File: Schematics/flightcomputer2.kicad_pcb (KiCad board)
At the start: 4 copper layers, 80 x 80 mm, 105 parts, among them J1 Microsemi_FlashPro-JTAG-10, J10 Pyro, J2 Pyro, J4 Drouge, J5 Conn_01x05_Pin, J6 Conn_01x05_Pin, J7 Conn_Coaxial_Small, J8 Micro_SD_Card, J9 USB_C_Receptacle_USB2.0_16P, Q1 IRLML2502TRPBF, Q2 IRLML2502TRPBF, Q3 BC817, Q4 IRLML2502TRPBF, Q6 Q_PMOS_GSD, SW1 SAMZO G4R0015010, SW2 SAMZO G4R0015010, U1 STM32F405RGT6, U2 SN65HVD230, U3 PowerIn, U4 LDL1117-3.3, U5 RFM95W-915S2, U6 Bosch BMP388, U7 LSM6DS3TR-C, U8 W25Q128JVP, U9 H3LIS331DL, Y1 8mhz

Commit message: dfm sent for ordering
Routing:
- net /FlashMemory/SPI_MOSI: track 42.3 -> 43.5 mm
- net /MCU/SWCLK: track 69.0 -> 68.0 mm
- net /GPS/GPS2_TX: track 41.0 -> 40.3 mm
- net /GPS/GPS2_RX: track 44.9 -> 44.2 mm
- net /GPS/RESET2: track 49.2 -> 49.8 mm
- net /GPS/RESET1: track 62.5 -> 62.0 mm
- net /FlashMemory/SPICLK: track 42.0 -> 41.5 mm
- net GND: track 153.8 -> 154.0 mm, vias 88 -> 87

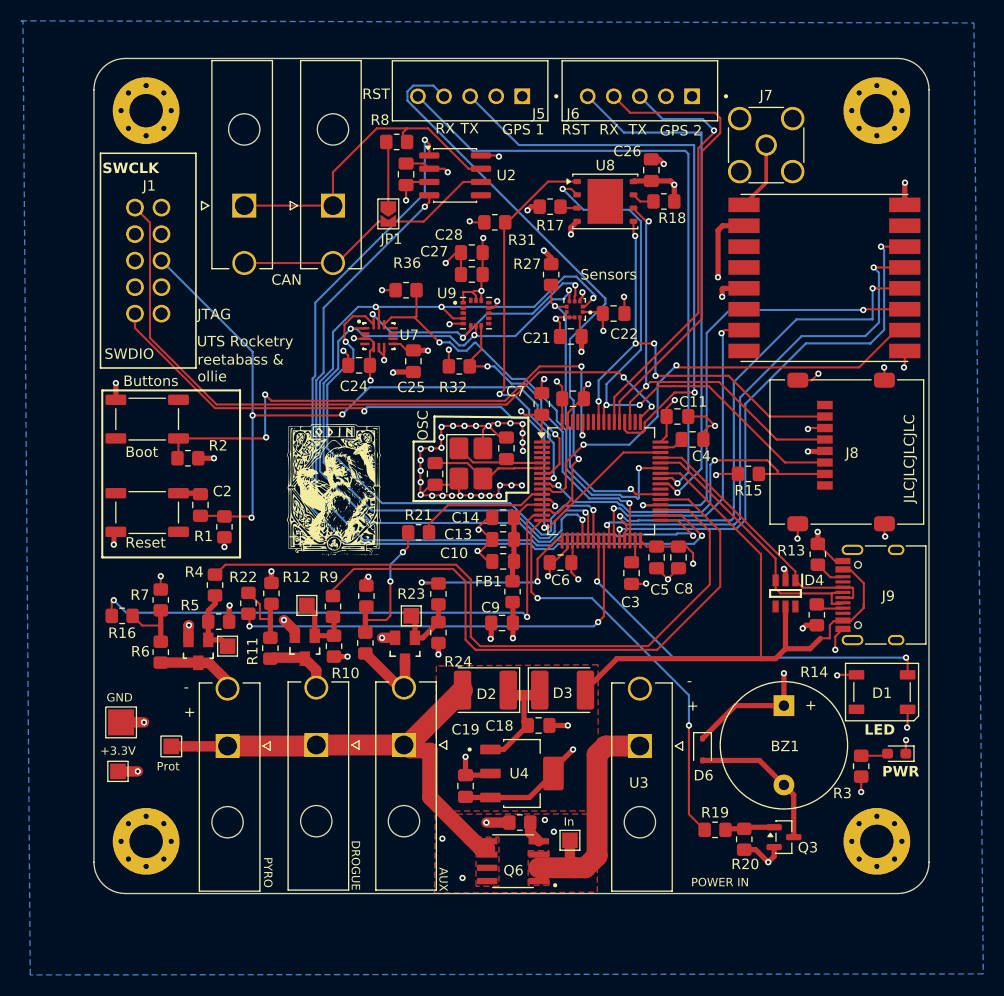
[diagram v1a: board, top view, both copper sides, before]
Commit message: added DIO0 and DIO2 pins to read lora module outputs
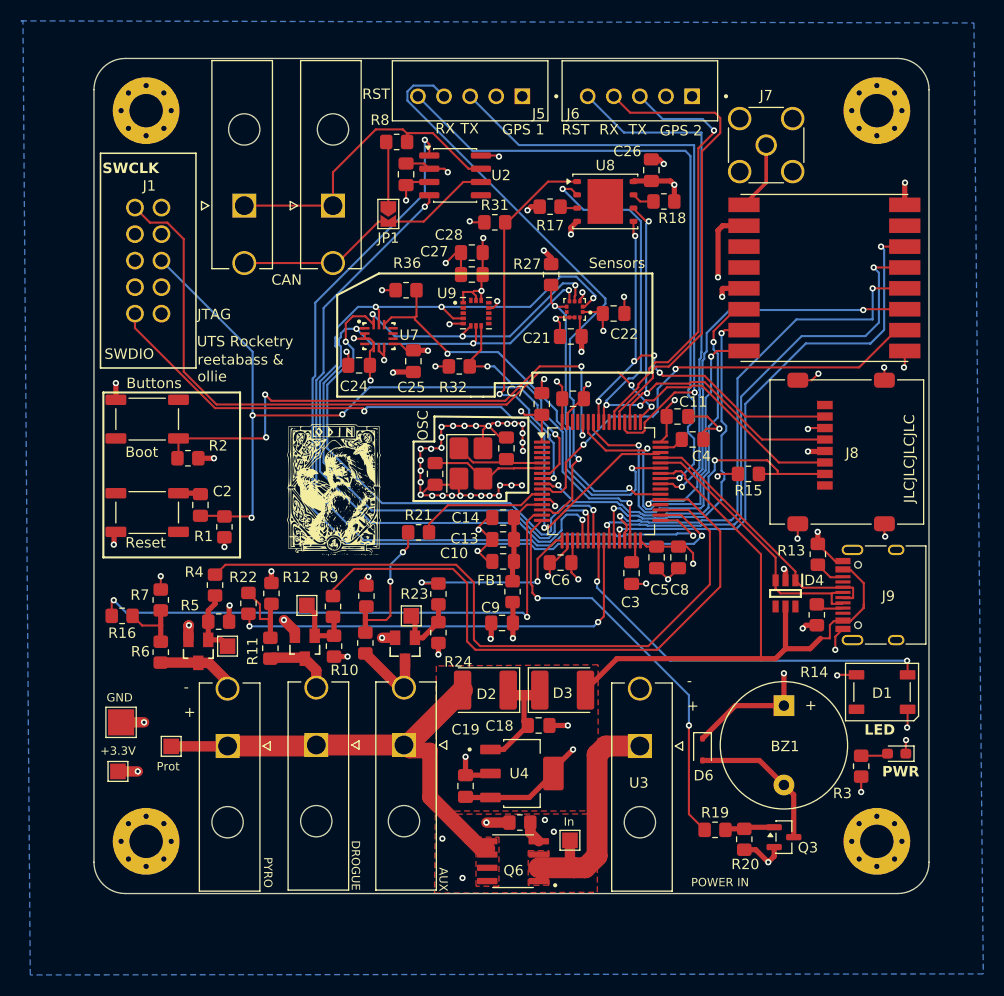
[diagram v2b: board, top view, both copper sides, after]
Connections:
- U1 pad 58: unconnected-(U1-PB6-Pad58) -> /LoRa/sxDIO0
- U1 pad 59: unconnected-(U1-PB7-Pad59) -> /LoRa/sxDIO2
- U5 pad 14: unconnected-(U5-DIO0-Pad14) -> /LoRa/sxDIO0
- U5 pad 16: unconnected-(U5-DIO2-Pad16) -> /LoRa/sxDIO2
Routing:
- net /LoRa/sxDIO0: track 0.00 -> 39.5 mm, vias 0 -> 2
- net /LoRa/sxDIO2: track 0.00 -> 36.9 mm, vias 0 -> 2
- net /LoRa/sxMOSI: track 43.8 -> 41.6 mm
- net /FlashMemory/SPI_MOSI: track 43.5 -> 42.3 mm
- net /MCU/SWCLK: track 68.0 -> 69.0 mm
- net /LoRa/sxDIO1: track 32.6 -> 33.3 mm
- net /GPS/GPS2_TX: track 40.3 -> 41.0 mm
- net /GPS/GPS2_RX: track 44.2 -> 44.9 mm
- net GND: track 154.0 -> 154.7 mm, vias 87 -> 88
- net /IMU/ChipSelectIMU: track 43.0 -> 42.3 mm
- net /LoRa/sxMIS0: track 43.9 -> 43.3 mm
- net /GPS/RESET1: track 62.0 -> 62.5 mm
- net /FlashMemory/SPICLK: track 41.5 -> 42.0 mm
- net /GPS/RESET2: track 49.8 -> 49.3 mm
